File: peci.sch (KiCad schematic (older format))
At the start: 5 parts

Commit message: initial footprint assignment and VERY rough placement
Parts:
- C701, C702: renamed from C?; footprint (none) -> Capacitor_SMD:C_0402_1005Metric
- R701, R702: renamed from R?; footprint (none) -> Resistor_SMD:R_0402_1005Metric
- U701: renamed from U?; footprint (none) -> Package_SO:MSOP-10_3x3mm_P0.5mm
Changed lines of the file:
@@
 $EndDescr
 $Comp
-L m2:MAX6621 U?
+L m2:MAX6621 U701
 U 1 1 5E1941AA
 P 4600 3600
-F 0 "U?" H 5000 3765 50  0000 C CNN
+F 0 "U701" H 5000 3765 50  0000 C CNN
 F 1 "MAX6621" H 5000 3674 50  0000 C CNN
-F 2 "" H 4600 3600 50  0001 C CNN
+F 2 "Package_SO:MSOP-10_3x3mm_P0.5mm" H 4600 3600 50  0001 C CNN
 F 3 "" H 4600 3600 50  0001 C CNN
 	1    4600 3600
@@
 Connection ~ 4400 4600
 $Comp
-L power:GND #PWR?
+L power:GND #PWR0701
 U 1 1 5E1949A9
 P 4400 4700
-F 0 "#PWR?" H 4400 4450 50  0001 C CNN
+F 0 "#PWR0701" H 4400 4450 50  0001 C CNN
 F 1 "GND" H 4405 4527 50  0000 C CNN
 F 2 "" H 4400 4700 50  0001 C CNN
@@
 	5600 4600 5150 4600
 $Comp
-L Device:C C?
+L Device:C C702
 U 1 1 5E19578C
 P 5600 4050
-F 0 "C?" H 5715 4096 50  0000 L CNN
+F 0 "C702" H 5715 4096 50  0000 L CNN
 F 1 "0.1u" H 5715 4005 50  0000 L CNN
-F 2 "" H 5638 3900 50  0001 C CNN
+F 2 "Capacitor_SMD:C_0402_1005Metric" H 5638 3900 50  0001 C CNN
 F 3 "~" H 5600 4050 50  0001 C CNN
 	1    5600 4050
@@
 PECI_GND
 $Comp
-L Device:C C?
+L Device:C C701
 U 1 1 5E196A84
 P 4000 4350
-F 0 "C?" H 4115 4396 50  0000 L CNN
+F 0 "C701" H 4115 4396 50  0000 L CNN
 F 1 "0.1u" H 4115 4305 50  0000 L CNN
-F 2 "" H 4038 4200 50  0001 C CNN
+F 2 "Capacitor_SMD:C_0402_1005Metric" H 4038 4200 50  0001 C CNN
 F 3 "~" H 4000 4350 50  0001 C CNN
 	1    4000 4350
@@
 	3800 4000 4400 4000
 $Comp
-L Device:R R?
+L Device:R R702
 U 1 1 5E194AD2
 P 5000 4600
-F 0 "R?" V 4900 4600 50  0000 C CNN
+F 0 "R702" V 4900 4600 50  0000 C CNN
 F 1 "0" V 5000 4600 50  0000 C CNN
-F 2 "" V 4930 4600 50  0001 C CNN
+F 2 "Resistor_SMD:R_0402_1005Metric" V 4930 4600 50  0001 C CNN
 F 3 "~" H 5000 4600 50  0001 C CNN
 	1    5000 4600
@@
 $EndComp
 $Comp
-L Device:R R?
+L Device:R R701
 U 1 1 5E19B2FB
 P 4150 3600
-F 0 "R?" V 4050 3600 50  0000 C CNN
+F 0 "R701" V 4050 3600 50  0000 C CNN
 F 1 "10k" V 4150 3600 50  0000 C CNN
-F 2 "" V 4080 3600 50  0001 C CNN
+F 2 "Resistor_SMD:R_0402_1005Metric" V 4080 3600 50  0001 C CNN
 F 3 "~" H 4150 3600 50  0001 C CNN
 	1    4150 3600

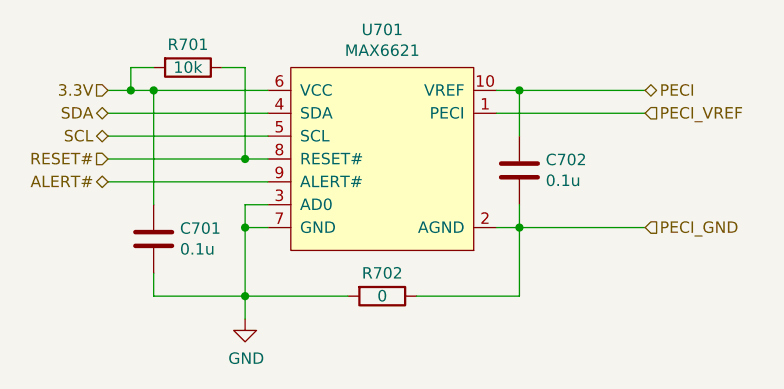
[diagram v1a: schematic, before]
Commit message: local component placement
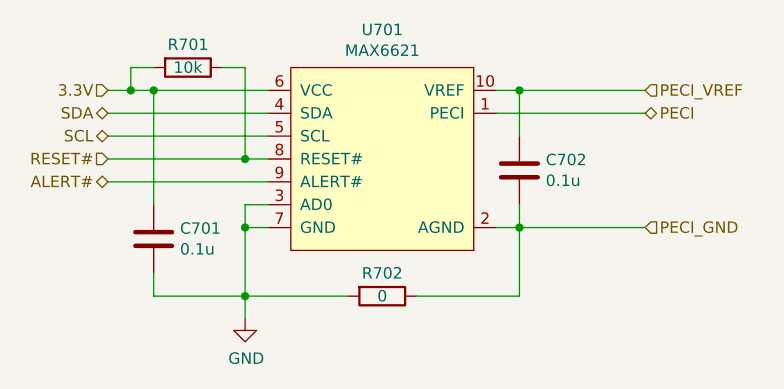
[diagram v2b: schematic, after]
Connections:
- net PECI: now also U701.1 (PECI); no longer C702.1, U701.10 (VREF)
- net PECI_VREF: now also C702.1, U701.10 (VREF); no longer U701.1 (PECI)
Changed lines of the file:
@@
 Wire Wire Line
 	5600 4300 6150 4300
-Text HLabel 6150 3700 2    50   BiDi ~ 0
+Text HLabel 6150 3800 2    50   BiDi ~ 0
 PECI
-Text HLabel 6150 3800 2    50   Input ~ 0
+Text HLabel 6150 3700 2    50   Input ~ 0
 PECI_VREF
 Text HLabel 6150 4300 2    50   Input ~ 0
